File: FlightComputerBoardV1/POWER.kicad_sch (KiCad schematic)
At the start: 69 parts, among them U14 TPS56A37RPAR, U15 LM74700, U16 INA260, U17 MCP9808_DFN, U18 LM74700, U21 PTPS2116DRLR, U22 TLV75533PDBVR, U7 TPS56A37RPAR

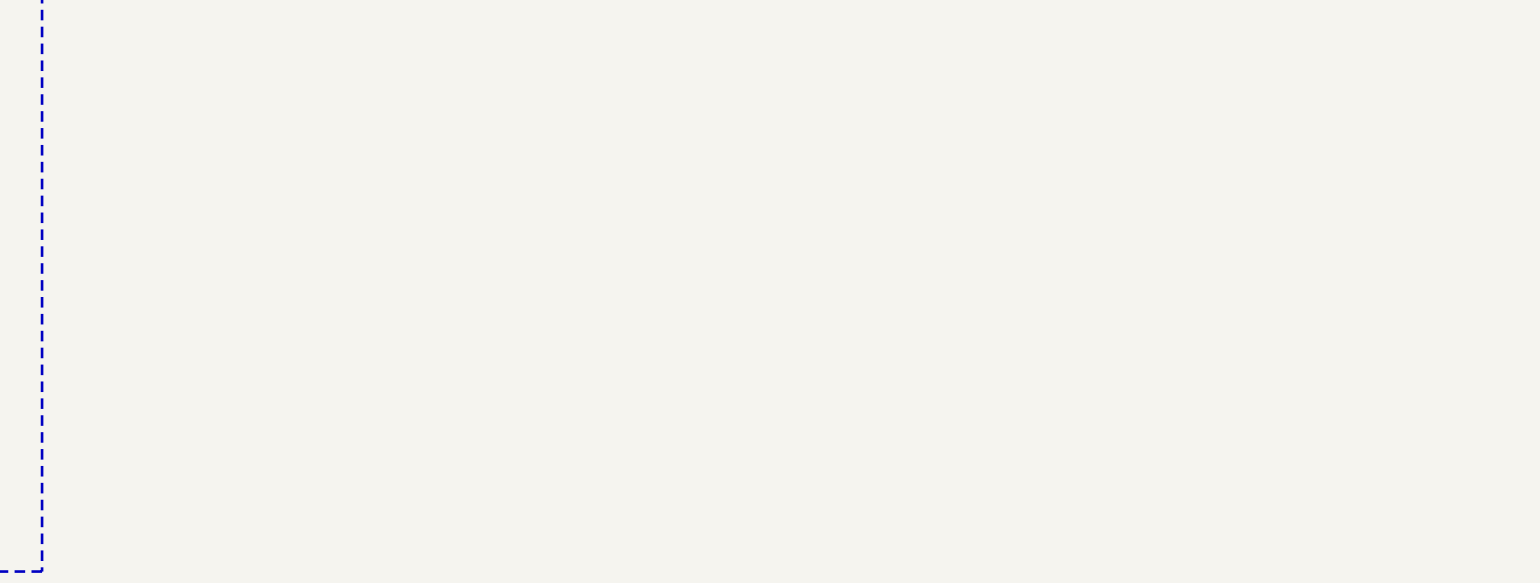
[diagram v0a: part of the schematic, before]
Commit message: Added 2 Linear Actuators
- Added symbols for ID10BT
- Added 2 ID10BTs to POWER sheet
- Added optocoupler and relay control circuit for ID10BTs
- Connected pins to MCU
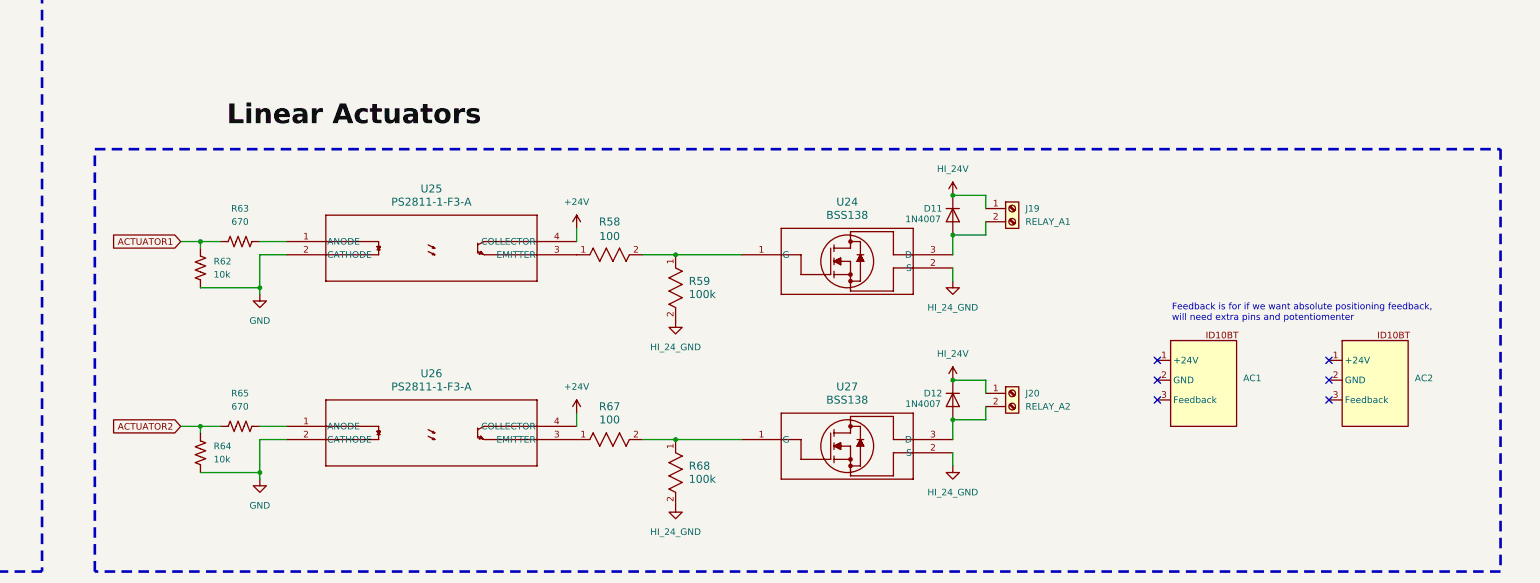
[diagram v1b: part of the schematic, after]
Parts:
- added AC1, AC2: (no value), Package_SO:SOIC-20W_7.5x12.8mm_P1.27mm, symbol FlightComputerBoardV1_Symbols:ID10BT
- added D11, D12: 1N4007, Diode_THT:D_DO-41_SOD81_P10.16mm_Horizontal, symbol Diode:1N4007
- added J19: RELAY_A1, symbol Connector:Screw_Terminal_01x02
- added J20: RELAY_A2, symbol Connector:Screw_Terminal_01x02
- added R58, R67: 100, RES_CRCW_0402, symbol FlightComputerBoardV1_Symbols:CRCW0402100RFKED
- added R59, R68: 100k, RC0402N_PAN, symbol FlightComputerBoardV1_Symbols:ERJ-2GEJ104X
- added R62, R64: 10k, symbol Device:R_US
- added R63, R65: 670, symbol Device:R_US
- added U24, U27: BSS138, SOT-23_3L_ONS, symbol FlightComputerBoardV1_Symbols:BSS138
- added U25, U26: PS2811-1-F3-A, PS2811-1_REN, symbol PS2811_1_F3_A:PS2811-1-F3-A
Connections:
- net +24V: now also U25.4 (COLLECTOR), U26.4 (COLLECTOR)
- net GND: now also R62.1, R64.1, U25.2 (CATHODE), U26.2 (CATHODE)
- new net: R65.2, U26.1 (ANODE)
- new net: R67.1, U26.3 (EMITTER)
- new net: R63.2, U25.1 (ANODE)
- new net: R58.1, U25.3 (EMITTER)
- new net: R58.2, R59.1, U24.1 (G)
- new net: D11.2 (A), J19.2 (Pin_2), U24.3 (D)
- new net: D12.2 (A), J20.2 (Pin_2), U27.3 (D)
- new net: R67.2, R68.1, U27.1 (G)
- new net ACTUATOR1: R62.2, R63.1
- new net ACTUATOR2: R64.2, R65.1
- new net HI_24V: D11.1 (K), D12.1 (K), J19.1 (Pin_1), J20.1 (Pin_1)
- new net HI_24_GND: R59.2, R68.2, U24.2 (S), U27.2 (S)
- no-connect marks 4 -> 10
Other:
- note added: "Feedback is for if we want absolute positioning feedback, will need extra pins and potentiomenter"

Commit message: added surge protection
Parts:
- added C86, C88: 47nF, symbol Device:C
- added C87: 0.1uF, symbol Device:C
- added C89: 680uF, symbol Device:C_Polarized
- added C90, C91, C92, C93: 100nF, symbol Device:C
- added CR3: SMAJ58A, SMASeries_LTF, symbol SMAJ58A:SMAJ58A
- added MOSFET3: FDB33N25TM, TO263_D2PAK_ONS, symbol FDB33N25TM:FDB33N25TM
- added R55: 10kOhm, symbol Device:R_US
- added R56: 90.9kOhm, symbol Device:R_US
- added R79: 374kOhm, symbol Device:R_US
- added R80, R96: 1kOhm, symbol Device:R_US
- added R95: 19kOhm, symbol Device:R_US
- added R97: 10Ohm, symbol Device:R_US
- added R98: 6.8mOhm, symbol Device:R_US
- added U23: LT4363IDE-2-PBF, DFN-12_DE_LIT, symbol LT4363IDE-2-PBF:LT4363IDE-2-PBF
- added U28, U30: INA260, Package_SO:TSSOP-16_4.4x5mm_P0.65mm, symbol Sensor_Energy:INA260
- added U29, U31: MCP9808_DFN, Package_DFN_QFN:DFN-8-1EP_3x2mm_P0.5mm_EP1.7x1.4mm, symbol Sensor_Temperature:MCP9808_DFN
- R43, R70: value 169kOhm -> 1MOhm
- R44, R71: value 36.1kOhm -> 100kOhm
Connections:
- net 3V3_USB is gone; now on net 3.3V_USB: C82.1, U21.6 (VIN2)
- net +24V: now also U28.1 (IN+), U28.12 (VBUS), U28.2 (IN+), U28.3 (IN+), U30.1 (IN+), U30.12 (VBUS), U30.2 (IN+), U30.3 (IN+); no longer C10.1, C11.1, C12.1, C36.1, C37.1, C38.1, R43.1, R70.1, U14.8 (VIN), U7.8 (VIN)
- net +3V3: now also C90.1, C91.1, C92.1, C93.1, U28.10 (VS), U29.8 (V_{DD}), U30.10 (VS), U31.8 (V_{DD})
- net GND: now also C86.2, C87.2, C88.2, C89.2, C90.2, C91.2, C92.2, C93.2, CR3.2, R55.2, R80.2, U23.13 (EPAD), U23.9 (GND), U28.11 (GND), U28.4 (A1), U28.5 (A0), U28.6 (GND), U29.4 (GND), U29.5 (A2), U29.6 (A1), U29.7 (A0), U29.9 (EP/GND), U30.11 (GND), U30.4 (A1), U30.5 (A0), U30.6 (GND), U31.4 (GND), U31.5 (A2), U31.6 (A1), U31.7 (A0), U31.9 (EP/GND)
- net LOAD_POWER_IN: now also U28.14 (IN-), U28.15 (IN-), U28.16 (IN-), U30.14 (IN-), U30.15 (IN-), U30.16 (IN-)
- net SCL_I2C_1: now also U28.9 (SCL), U29.2 (SCL), U30.9 (SCL), U31.2 (SCL)
- net SDA_I2C_1: now also U28.8 (SDA), U29.1 (SDA), U30.8 (SDA), U31.1 (SDA)
- net EN_Bucks: now reaches R70.2, R71.1, U14.1 (EN)
- net EN_Bucks: now also R43.2, R44.1, U7.1 (EN), U23.11 (ENOUT)
- net +3.3V_Buck renamed 3.3V_Buck
- net +3V renamed 3.3V_Combined
- net +3V3_USB renamed 3.3V_USB
- net +5V_Buck renamed 5V_Buck
- net Output renamed 24V_Unprotected
- net 24V_Unprotected: now also MOSFET3.2 (D), R79.1, R96.1
- new net: C88.1, R97.2, U23.4 (GATE)
- new net: MOSFET3.1 (G), R97.1
- new net: MOSFET3.3 (S), R98.1, U23.3 (SNS)
- new net: R80.1, R95.2, U23.1 (FB)
- new net: C86.1, U23.12 (TMR)
- new net: C87.1, CR3.1, R96.2, U23.5 (VCC), U23.6 (*SHDN)
- new net: R55.1, R56.2, U23.7 (OV)
- new net: R56.1, R79.2, U23.8 (UV)
- new net 24V_Protected: C10.1, C11.1, C12.1, C36.1, C37.1, C38.1, C89.1, R43.1, R70.1, R95.1, R98.2, U14.8 (VIN), U23.2 (OUT), U7.8 (VIN)
- no-connect marks 10 -> 15
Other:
- moved on the sheet: AC1, AC2, C10, C11, C12, C13, C14, C15, C16, C17, C18, C19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

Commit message: finished surge
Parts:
- removed MOSFET3: FDB33N25TM, TO263_D2PAK_ONS, symbol FDB33N25TM:FDB33N25TM
- added MOSFET3: PSMN4R8-100BSEJ, D2PAK_SOT404_NEX, symbol PSMN4R8-100BSE:PSMN4R8-100BSEJ
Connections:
- net +24V: no longer U16.1 (IN+), U16.12 (VBUS), U16.2 (IN+), U16.3 (IN+), U28.1 (IN+), U28.12 (VBUS), U28.2 (IN+), U28.3 (IN+), U30.1 (IN+), U30.12 (VBUS), U30.2 (IN+), U30.3 (IN+)
- net 24V_Protected: now also U16.1 (IN+), U16.12 (VBUS), U16.2 (IN+), U16.3 (IN+); no longer C10.1, C11.1, C12.1, C36.1, C37.1, C38.1, R43.1, R70.1, U14.8 (VIN), U7.8 (VIN)
- net 24V_Unprotected: now also MOSFET3.2 (D)
- net 3.3V_Buck: now also U30.1 (IN+), U30.12 (VBUS), U30.2 (IN+), U30.3 (IN+); no longer C81.1, R53.1, U21.3 (VIN1), U21.5 (MODE)
- net 5V_Buck: now also U28.1 (IN+), U28.12 (VBUS), U28.2 (IN+), U28.3 (IN+)
- net at R97.1: now also MOSFET3.1 (G)
- net at R98.1, U23.3 (SNS): now also MOSFET3.3 (S)
- net 3.3V_Combined renamed +3.3V
- removed net LOAD_POWER_IN: U16.14 (IN-), U16.15 (IN-), U16.16 (IN-), U28.14 (IN-), U28.15 (IN-), U28.16 (IN-), U30.14 (IN-), U30.15 (IN-), U30.16 (IN-)
- new net 24V_Protected_Out: C10.1, C11.1, C12.1, C36.1, C37.1, C38.1, R43.1, R70.1, U14.8 (VIN), U7.8 (VIN)
- new net 24_Protected_Out: U16.14 (IN-), U16.15 (IN-), U16.16 (IN-)
- new net 3.3V_Buck_Out: C81.1, R53.1, U21.3 (VIN1), U21.5 (MODE), U30.14 (IN-), U30.15 (IN-), U30.16 (IN-)
- new net 5V_Buck_Out: U28.14 (IN-), U28.15 (IN-), U28.16 (IN-)
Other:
- moved on the sheet: R53, R54

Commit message: new switching architecture, new surge protection
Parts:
- added C100, C102, C96, C97, C98: 100nF, UF_20_ADI, symbol Device:C
- added C101, C103: 6.8nF, UF_20_ADI, symbol Device:C
- added C104, C99: 47uF, UF_20_ADI, symbol Device:C_Polarized
- added C105: 10uF, UF_20_ADI, symbol Device:C_Polarized
- added C106: 0.1uF, symbol Device:C
- added C107, C108: 47nF, symbol Device:C
- added C109: 680uF, symbol Device:C_Polarized
- added CR4: SMAJ58A, SMASeries_LTF, symbol SMAJ58A:SMAJ58A
- added MOSFET4: PSMN4R8-100BSEJ, D2PAK_SOT404_NEX, symbol PSMN4R8-100BSE:PSMN4R8-100BSEJ
- added Q10, Q7, Q8, Q9: FDD4685, TO252_FDD_ONS, symbol FDD4685:FDD4685
- added R100: 158kOhm, Resistor_THT:R_Array_SIP4, symbol Device:R_US
- added R101, R105: 34.8kOhm, Resistor_THT:R_Array_SIP4, symbol Device:R_US
- added R102, R104: 1.87MOhm, Resistor_THT:R_Array_SIP4, symbol Device:R_US
- added R103, R106: 68.1kOhm, Resistor_THT:R_Array_SIP4, symbol Device:R_US
- added R107: 100kOhm, Resistor_THT:R_Array_SIP4, symbol Device:R_US
- added R108, R109: 133Ohm, Resistor_THT:R_Array_SIP4, symbol Device:R_US
- added R110, R117: 1kOhm, symbol Device:R_US
- added R111: 374kOhm, symbol Device:R_US
- added R112: 90.9kOhm, symbol Device:R_US
- added R113: 10kOhm, symbol Device:R_US
- added R114: 10Ohm, symbol Device:R_US
- added R115: 6.8mOhm, symbol Device:R_US
- added R116: 19kOhm, symbol Device:R_US
- added U33: LTC4418IUF-TRPBF, UF_20_ADI, symbol LTC4418:LTC4418IUF-TRPBF
- added U34, U35: BAT46WJ_115, SC-90_SOD323F_NEX, symbol BAT46WJ115:BAT46WJ_115
- added U36: LT4363IDE-2-PBF, DFN-12_DE_LIT, symbol LT4363IDE-2-PBF:LT4363IDE-2-PBF
- C47, C48, C49, C52, C53, C54, CR1, CR2, MOSFET1, MOSFET2, U15, U18: now not fitted
- R43, R70: value 1MOhm -> 169kOhm
- R44, R71: value 100kOhm -> 36.1kOhm
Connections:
- net 24V_Protected_Out is gone; now on net 24V_Protected: C10.1, C11.1, C12.1, C36.1, C37.1, C38.1, R43.1, R70.1, U14.8 (VIN), U7.8 (VIN)
- net +3.3V: now also R107.2
- net 24V_Protected: now also C101.1, C103.1, C105.1, Q10.2 (D), Q8.2 (D), U33.15 (VOUT); no longer C89.1, R95.1, R98.2, U23.2 (OUT)
- net 24V_Unprotected: no longer MOSFET3.2 (D), R79.1, R96.1
- net 3.3V_Buck: now also C81.1, R53.1, U21.3 (VIN1), U21.5 (MODE)
- net 3.3V_Buck_Out: no longer C81.1, R53.1, U21.3 (VIN1), U21.5 (MODE)
- net GND: now also C100.2, C102.2, C104.2, C105.2, C106.2, C107.2, C108.2, C109.2, C96.2, C97.2, C98.2, C99.2, CR4.2, R100.2, R103.1, R106.1, R113.2, R117.2, U33.21 (GND), U33.8 (GND), U36.13 (EPAD), U36.9 (GND)
- removed net EN_Bucks: R43.2, R44.1, R70.2, R71.1, U14.1 (EN), U23.11 (ENOUT), U7.1 (EN)
- new net: C106.1, CR4.1, R110.2, U36.5 (VCC), U36.6 (*SHDN)
- new net: C101.2, Q7.1 (G), Q8.1 (G), R108.2, U34.1
- new net: R108.1, U33.11 (G2), U34.2
- new net: R70.2, R71.1, U14.1 (EN)
- new net: R107.1, U33.6 (*VALID1)
- new net: R101.2, R102.1, U33.4 (UV2)
- new net: R105.1, R106.2, U33.3 (OV1), U33.7 (*VALID2)
- new net: R43.2, R44.1, U7.1 (EN)
- new net: C96.1, U33.1 (TMR), U33.10 (INTVCC), U33.18 (EN), U33.19 (*SHDN)
- new net: C103.2, Q10.1 (G), Q9.1 (G), R109.2, U35.1
- new net: R109.1, U33.13 (G1), U35.2
- new net: MOSFET4.1 (G), R114.1
- new net: MOSFET4.3 (S), R115.1, U36.3 (SNS)
- new net: C100.1, Q7.3 (S), Q8.3 (S), U33.12 (VS2)
- new net: C102.1, Q10.3 (S), Q9.3 (S), U33.14 (VS1)
- new net: R104.1, R105.2, U33.2 (UV1)
- new net: R100.1, U33.20 (HYS)
- new net: R101.1, R103.2, U33.5 (OV2)
- new net: C107.1, R114.2, U36.4 (GATE)
- new net: C108.1, U36.12 (TMR)
- new net: R116.2, R117.1, U36.1 (FB)
- new net: R112.2, R113.1, U36.7 (OV)
- new net: R111.2, R112.1, U36.8 (UV)
- new net Battery_24V_Protected: C89.1, C97.1, C99.1, Q7.2 (D), R102.2, R95.1, R98.2, U23.2 (OUT), U33.16 (V2)
- new net Battery_24V_Unprotected: MOSFET3.2 (D), R79.1, R96.1
- new net Wall_24V_Protected: C104.1, C109.1, C98.1, Q9.2 (D), R104.2, R115.2, R116.1, U33.17 (V1), U36.2 (OUT)
- new net Wall_24V_Unprotected: MOSFET4.2 (D), R110.1, R111.1
- no-connect marks 15 -> 19
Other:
- moved on the sheet: AC1, AC2, C50, C51, C86, C87, C88, C89, C90, C91, C92, C93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

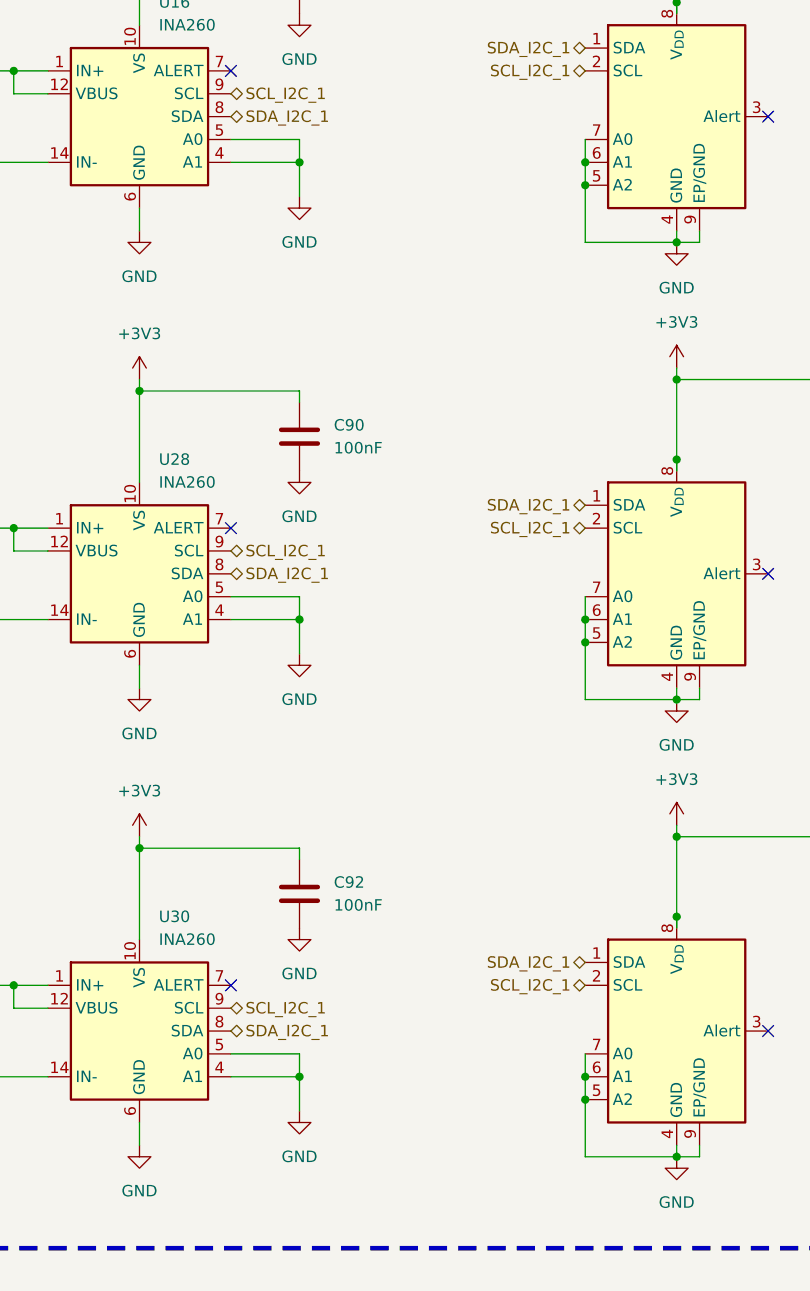
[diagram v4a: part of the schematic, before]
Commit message: added addresses
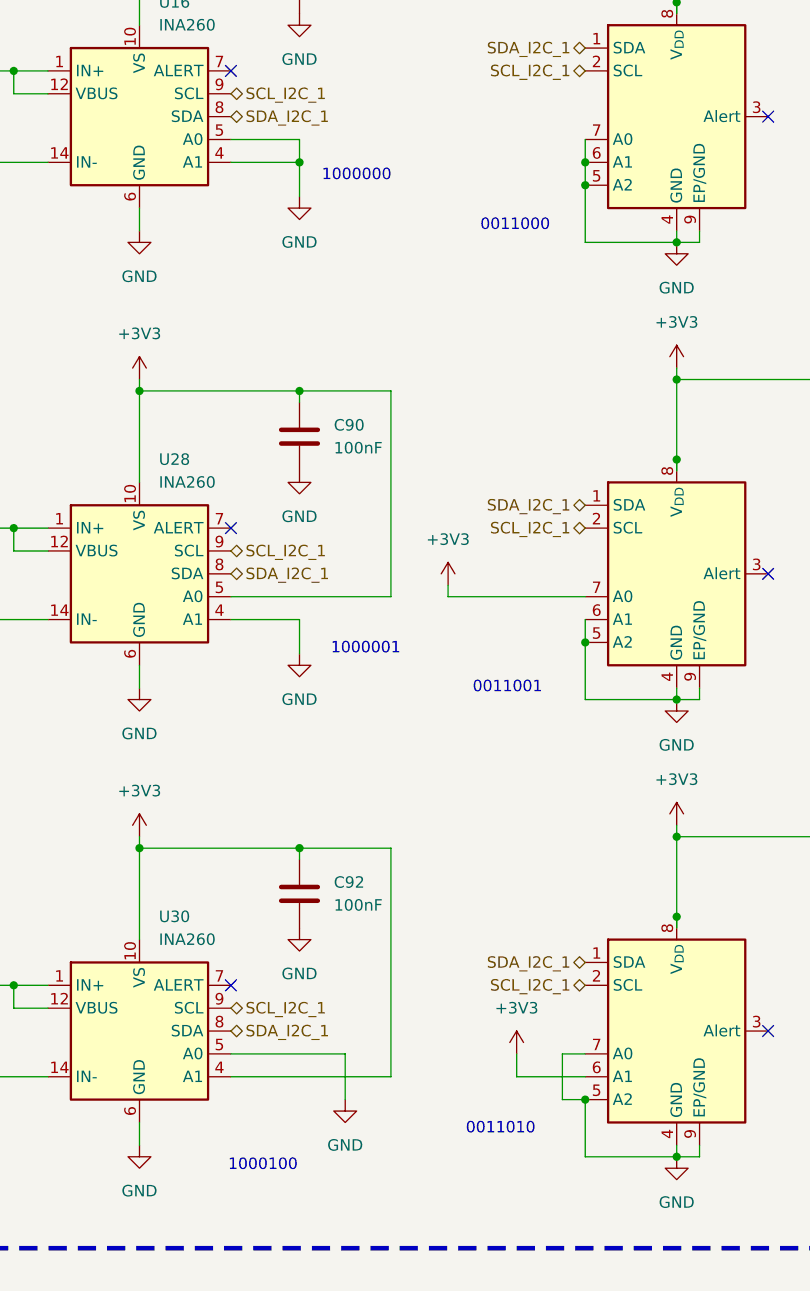
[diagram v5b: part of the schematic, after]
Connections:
- net +3V3: now also U28.5 (A0), U29.7 (A0), U30.4 (A1), U31.6 (A1)
- net GND: no longer U28.5 (A0), U29.7 (A0), U30.4 (A1), U31.6 (A1)
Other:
- note added: "0011000"
- note added: "0011001"
- note added: "0011010"
- note added: "1000000"
- note added: "1000001"
- note added: "1000100"

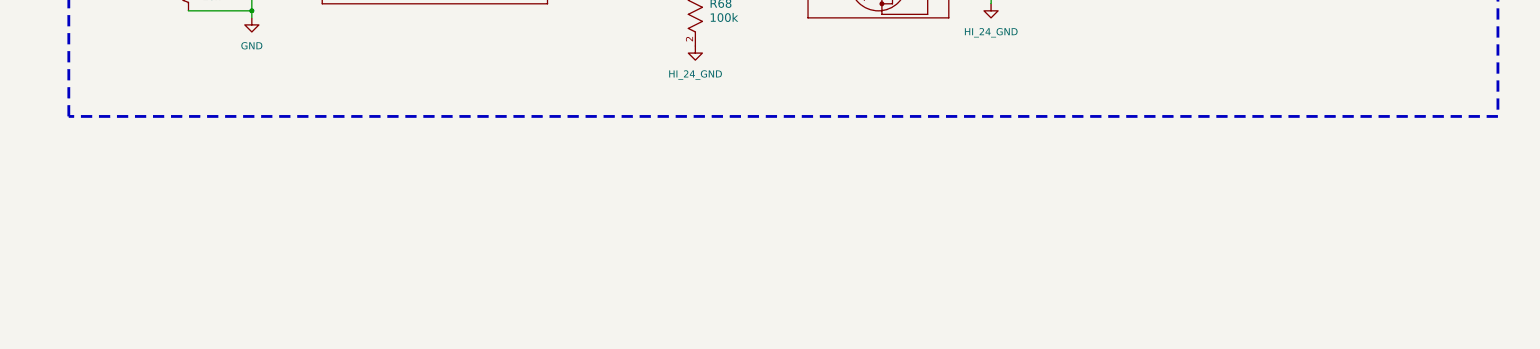
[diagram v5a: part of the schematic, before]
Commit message: Late night shenanigans
- Added radar module sheet
- Created symbols for: radar, RFD900xus
- Added RFD900xus
- Fixed PT voltage dividers
To do:
- Add decoupling and test points
- Finish finding appropriate gate driver for H bridge linear actuator circuit
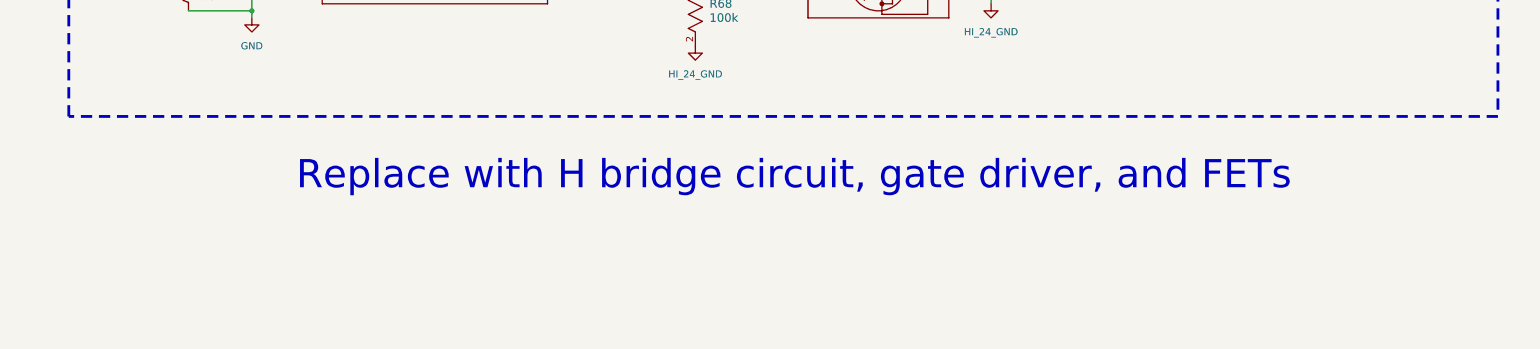
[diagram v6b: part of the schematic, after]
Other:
- note added: "Replace with H bridge circuit, gate driver, and FETs"
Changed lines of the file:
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@@
+		)
+	)
+	(text "Replace with H bridge circuit, gate driver, and FETs"
+		(exclude_from_sim no)
+		(at 387.35 283.718 0)
+		(effects
+			(font
+				(face "Arial")
+				(size 5.08 5.08)
+				(color 255 0 0 1)
+			)
 		)
 	)
